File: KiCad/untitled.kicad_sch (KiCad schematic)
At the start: 11 parts, among them J5 Power, U1 TL072, U2 TL072

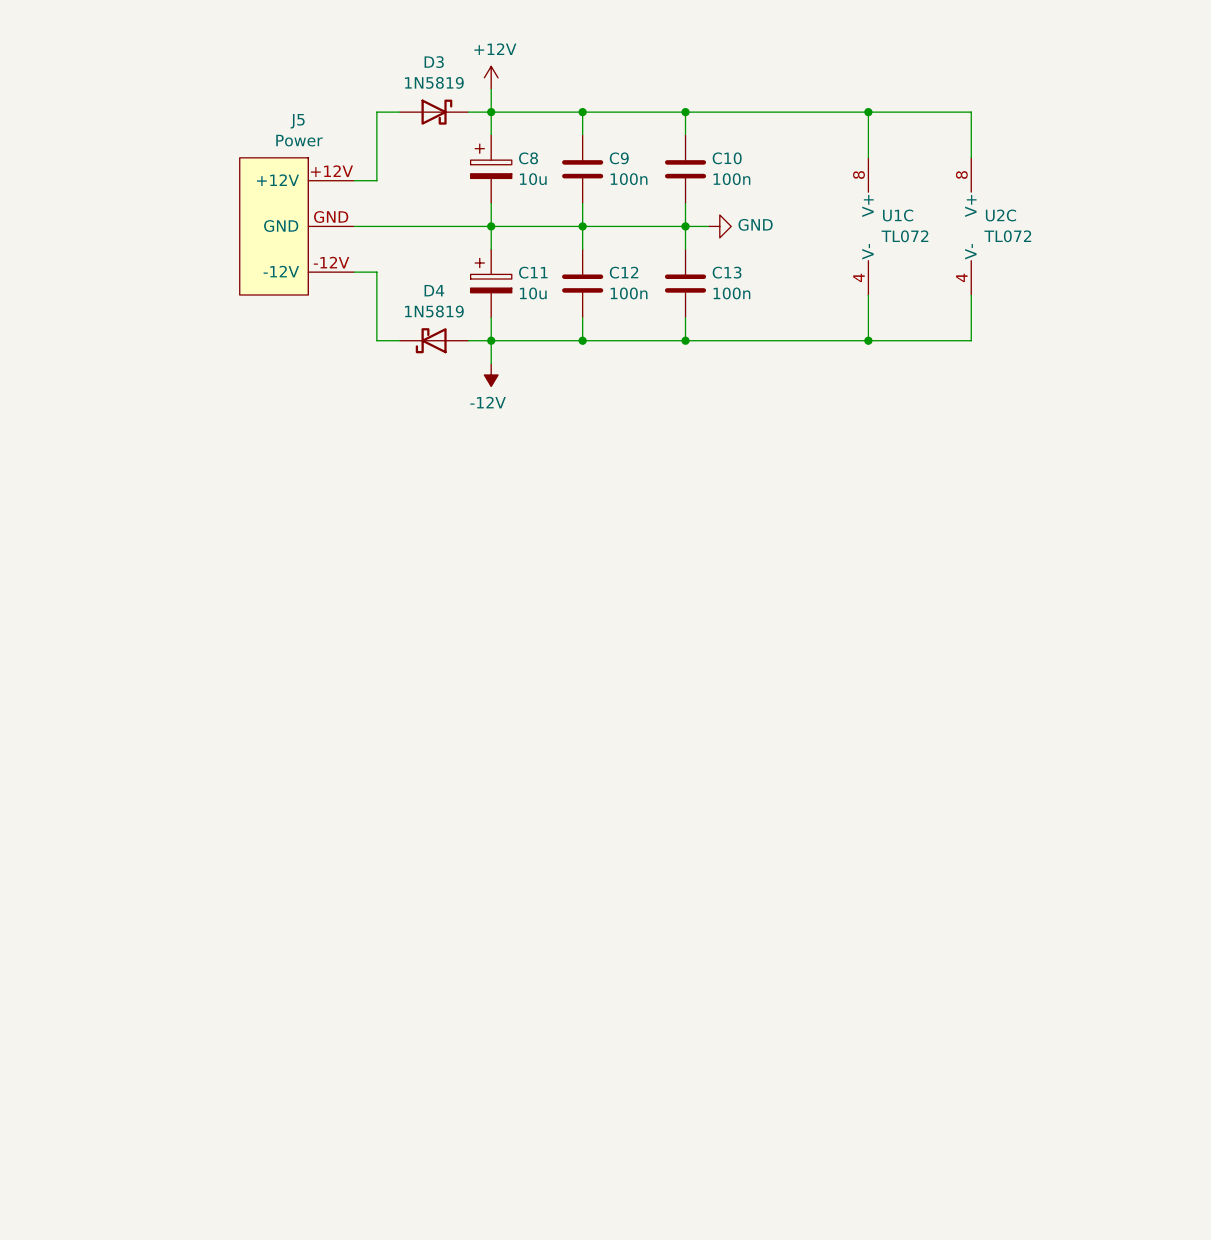
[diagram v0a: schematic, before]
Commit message: Added new Powerrail and fixed ERC Error
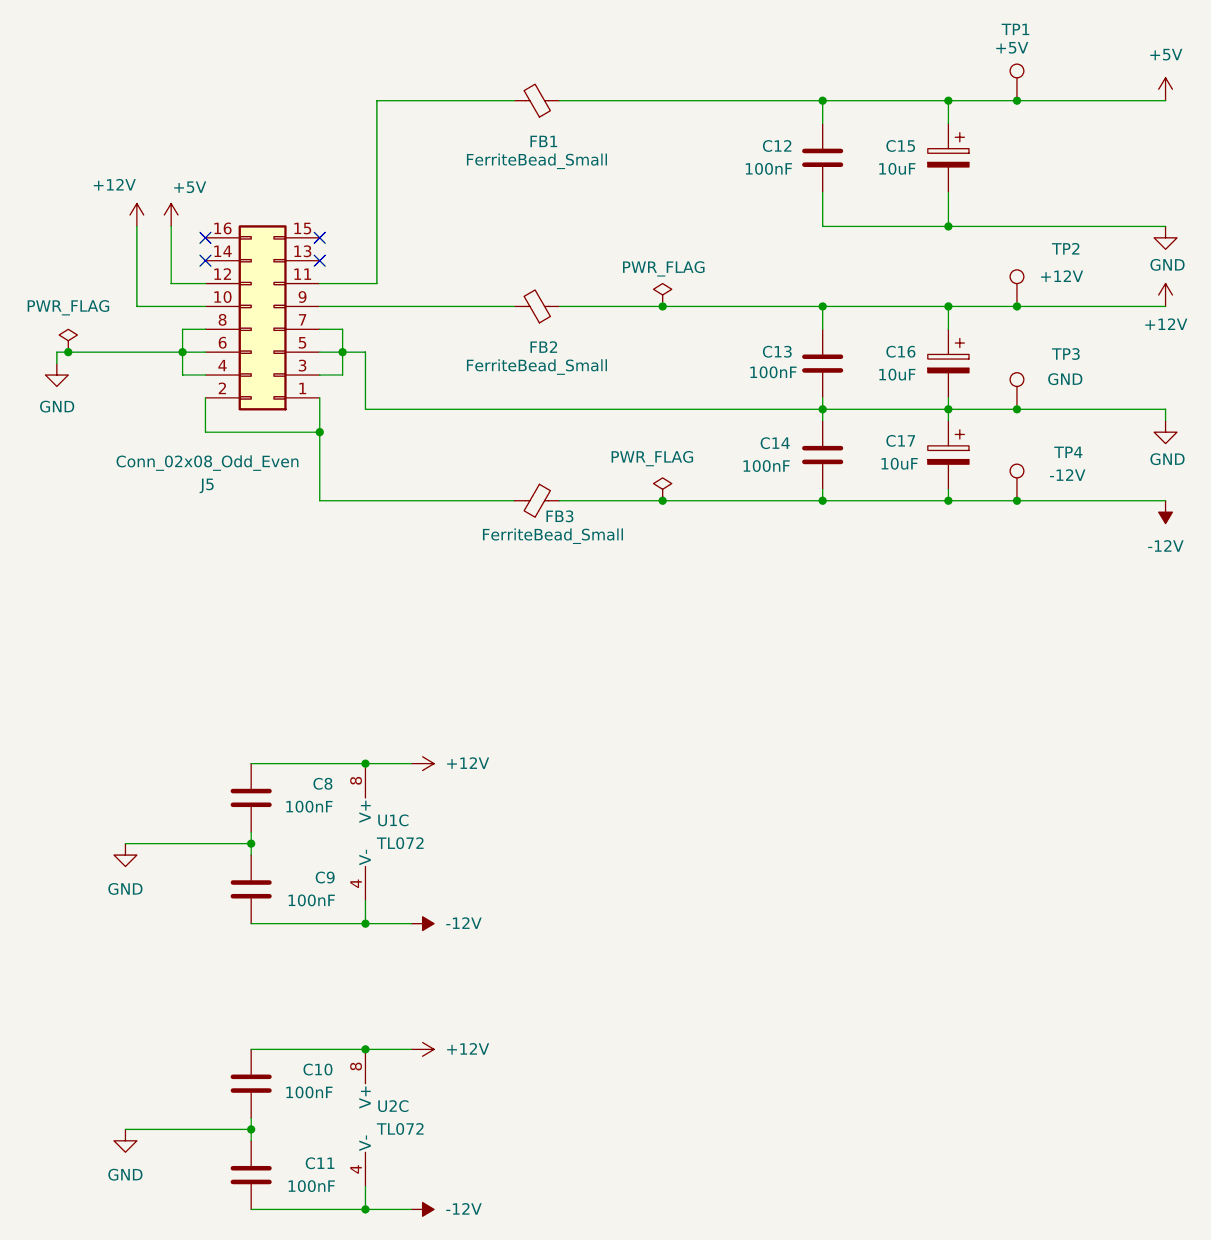
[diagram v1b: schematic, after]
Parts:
- removed C11, C8: 10u, Capacitor_Tantalum_SMD:CP_EIA-3216-18_Kemet-A, symbol Device:C_Polarized
- removed D3, D4: 1N5819, Diode_SMD:D_SOD-323, symbol Diode:1N5817
- removed J5: Power, CATs_Eurosynth_Specials:Power_2x5_Vertical, symbol Eurorack_Synth:Power_2x5
- added C11, C14, C8: 100nF, Capacitor_SMD:C_0805_2012Metric_Pad1.18x1.45mm_HandSolder, symbol Device:C
- added C15, C16, C17: 10uF, Capacitor_SMD:CP_Elec_5x5.4, symbol Device:C_Polarized
- added FB1, FB2, FB3: FerriteBead_Small, Inductor_SMD:L_0805_2012Metric_Pad1.05x1.20mm_HandSolder, symbol Device:FerriteBead_Small
- added J5: Conn_02x08_Odd_Even, symbol Connector_Generic:Conn_02x08_Odd_Even
- added TP1: +5V, TestPoint:TestPoint_Pad_D1.5mm, symbol Connector:TestPoint
- added TP2: +12V, TestPoint:TestPoint_Pad_D1.5mm, symbol Connector:TestPoint
- added TP3: GND, TestPoint:TestPoint_Pad_D1.5mm, symbol Connector:TestPoint
- added TP4: -12V, TestPoint:TestPoint_Pad_D1.5mm, symbol Connector:TestPoint
- C10, C12, C13, C9: value 100n -> 100nF; footprint Capacitor_SMD:C_0402_1005Metric -> Capacitor_SMD:C_0805_2012Metric_Pad1.18x1.45mm_HandSolder; LCSC C1525 -> (none)
- U1, U2: footprint Package_SO:SOIC-8_3.9x4.9mm_P1.27mm -> (none); LCSC C6961 -> (none)
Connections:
- net +12V: now also C10.1, C13.1, C16.1, C8.1, FB2.1, J5.10 (Pin_10), TP2.1; no longer C10.2, C9.2
- net -12V: now also C9.2, C11.2, C14.2, C17.2, FB3.1, TP4.1; no longer C12.1, C13.1
- net GND: now also C10.2, C11.1, C14.1, C15.2, C16.2, C17.1, C8.2, J5.3 (Pin_3), J5.4 (Pin_4), J5.5 (Pin_5), J5.6 (Pin_6), J5.7 (Pin_7), J5.8 (Pin_8), TP3.1; no longer C10.1
- new net: FB2.2, J5.9 (Pin_9)
- new net: FB3.2, J5.1 (Pin_1), J5.2 (Pin_2)
- new net: FB1.2, J5.11 (Pin_11)
- new net +5V: C12.1, C15.1, FB1.1, J5.12 (Pin_12), TP1.1
- no-connect marks 0 -> 4
